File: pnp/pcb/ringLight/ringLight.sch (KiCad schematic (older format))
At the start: 13 parts, among them J1 Conn_01x03_Male, J2 Conn_01x03_Male

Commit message: Add LCSC PNs to Ringlight
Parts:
- J1: LCSC (none) -> C146126
- J2: LCSC (none) -> C141812
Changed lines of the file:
@@
 F 2 "Connector_JST:JST_PH_B3B-PH-SM4-TB_1x03-1MP_P2.00mm_Vertical" H 1050 1150 50  0001 C CNN
 F 3 "~" H 1050 1150 50  0001 C CNN
+F 4 "C141812" H 1050 1150 50  0001 C CNN "LCSC"
 	1    1050 1150
 	1    0    0    -1
@@
 F 2 "Connector_JST:JST_PH_B3B-PH-SM4-TB_1x03-1MP_P2.00mm_Vertical" H 725 1150 50  0001 C CNN
 F 3 "~" H 725 1150 50  0001 C CNN
+F 4 "C146126" H 725 1150 50  0001 C CNN "LCSC"
 	1    725  1150
 	1    0    0    -1

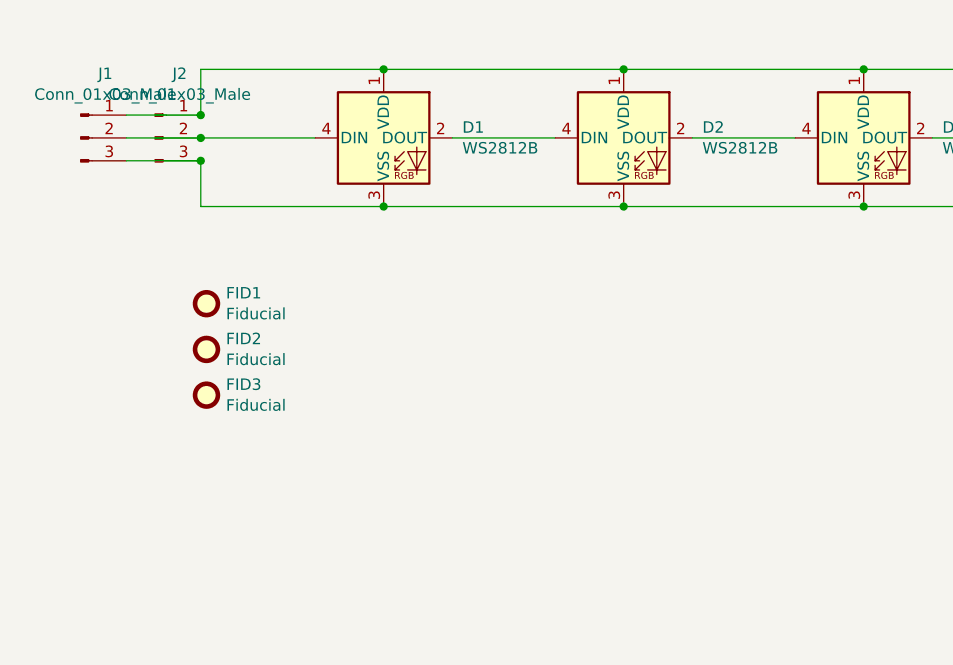
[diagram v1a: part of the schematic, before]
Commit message: updated ring light to rev03. changed connector pinout to match motherboard. switched to THT for connector that works with both right angle and straight up to be compatible with both board orientations. increased fiducial size. added decoupling capacitor.
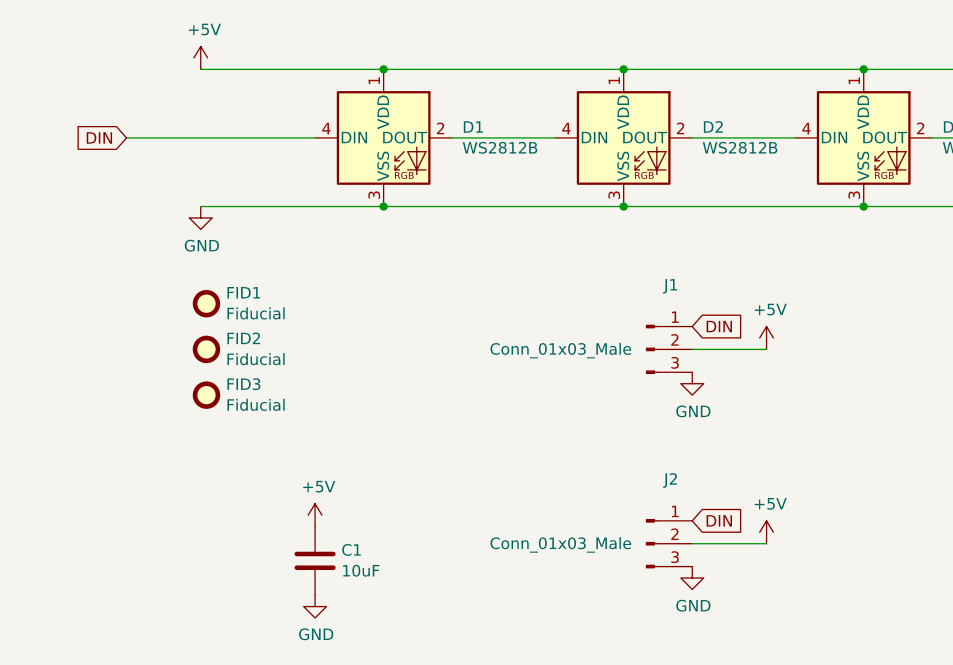
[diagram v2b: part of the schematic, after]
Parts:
- added C1: 10uF, Capacitor_SMD:C_0805_2012Metric, symbol Device:C
- FID1, FID2, FID3: footprint Fiducial:Fiducial_0.5mm_Mask1mm -> Fiducial:Fiducial_1mm_Mask2mm
- J1: footprint Connector_JST:JST_PH_B3B-PH-SM4-TB_1x03-1MP_P2.00mm_Vertical -> Connector_JST:JST_XH_B3B-XH-A_1x03_P2.50mm_Vertical
- J2: footprint Connector_JST:JST_PH_B3B-PH-SM4-TB_1x03-1MP_P2.00mm_Vertical -> index:S3B-XH-SM4-TB
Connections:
- net +5V: now reaches D1.1 (VDD), D2.1 (VDD), D3.1 (VDD), D4.1 (VDD), D5.1 (VDD), D6.1 (VDD), D7.1 (VDD), D8.1 (VDD)
- net +5V: now also J1.2 (Pin_2), J2.2 (Pin_2), C1.1; no longer J1.1 (Pin_1), J2.1 (Pin_1)
- net GND: now reaches D1.3 (VSS), D2.3 (VSS), D3.3 (VSS), D4.3 (VSS), D5.3 (VSS), D6.3 (VSS), D7.3 (VSS), D8.3 (VSS), J1.3 (Pin_3), J2.3 (Pin_3)
- net GND: now also C1.2
- new net DIN: D1.4 (DIN), J1.1 (Pin_1), J2.1 (Pin_1)
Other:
- moved on the sheet: J1, J2
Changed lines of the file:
@@
 L Connector:Conn_01x03_Male J2
 U 1 1 5EDD8ED7
-P 1050 1150
-F 0 "J2" H 1158 1431 50  0000 C CNN
-F 1 "Conn_01x03_Male" H 1158 1340 50  0000 C CNN
-F 2 "Connector_JST:JST_PH_B3B-PH-SM4-TB_1x03-1MP_P2.00mm_Vertical" H 1050 1150 50  0001 C CNN
-F 3 "~" H 1050 1150 50  0001 C CNN
-F 4 "C141812" H 1050 1150 50  0001 C CNN "LCSC"
-	1    1050 1150
+P 3200 2925
+F 0 "J2" H 3308 3206 50  0000 C CNN
+F 1 "Conn_01x03_Male" H 2825 2925 50  0000 C CNN
+F 2 "index:S3B-XH-SM4-TB" H 3200 2925 50  0001 C CNN
+F 3 "~" H 3200 2925 50  0001 C CNN
+F 4 "C141812" H 3200 2925 50  0001 C CNN "LCSC"
+	1    3200 2925
 	1    0    0    -1
 $EndComp
@@
 $EndComp
 Wire Wire Line
-	1250 1150 1750 1150
-Wire Wire Line
-	1250 1250 1250 1450
-Wire Wire Line
 	1250 1450 2050 1450
 Wire Wire Line
@@
 Wire Wire Line
 	8650 1150 9100 1150
-Wire Wire Line
-	1250 850  1250 1050
 $Comp
 L Mechanical:Fiducial FID1
@@
 F 0 "FID1" H 1360 1921 50  0000 L CNN
 F 1 "Fiducial" H 1360 1830 50  0000 L CNN
-F 2 "Fiducial:Fiducial_0.5mm_Mask1mm" H 1275 1875 50  0001 C CNN
+F 2 "Fiducial:Fiducial_1mm_Mask2mm" H 1275 1875 50  0001 C CNN
 F 3 "~" H 1275 1875 50  0001 C CNN
 	1    1275 1875
@@
 F 0 "FID2" H 1360 2121 50  0000 L CNN
 F 1 "Fiducial" H 1360 2030 50  0000 L CNN
-F 2 "Fiducial:Fiducial_0.5mm_Mask1mm" H 1275 2075 50  0001 C CNN
+F 2 "Fiducial:Fiducial_1mm_Mask2mm" H 1275 2075 50  0001 C CNN
 F 3 "~" H 1275 2075 50  0001 C CNN
 	1    1275 2075
@@
 F 0 "FID3" H 1360 2321 50  0000 L CNN
 F 1 "Fiducial" H 1360 2230 50  0000 L CNN
-F 2 "Fiducial:Fiducial_0.5mm_Mask1mm" H 1275 2275 50  0001 C CNN
+F 2 "Fiducial:Fiducial_1mm_Mask2mm" H 1275 2275 50  0001 C CNN
 F 3 "~" H 1275 2275 50  0001 C CNN
 	1    1275 2275
@@
 L Connector:Conn_01x03_Male J1
 U 1 1 607E080D
-P 725 1150
-F 0 "J1" H 833 1431 50  0000 C CNN
-F 1 "Conn_01x03_Male" H 833 1340 50  0000 C CNN
-F 2 "Connector_JST:JST_PH_B3B-PH-SM4-TB_1x03-1MP_P2.00mm_Vertical" H 725 1150 50  0001 C CNN
-F 3 "~" H 725 1150 50  0001 C CNN
-F 4 "C146126" H 725 1150 50  0001 C CNN "LCSC"
-	1    725  1150
-	1    0    0    -1
-$EndComp
-Wire Wire Line
-	925  1050 1250 1050
-Connection ~ 1250 1050
-Wire Wire Line
-	925  1150 1250 1150
-Connection ~ 1250 1150
-Wire Wire Line
-	925  1250 1250 1250
-Connection ~ 1250 1250
+P 3200 2075
+F 0 "J1" H 3308 2356 50  0000 C CNN
+F 1 "Conn_01x03_Male" H 2825 2075 50  0000 C CNN
+F 2 "Connector_JST:JST_XH_B3B-XH-A_1x03_P2.50mm_Vertical" H 3200 2075 50  0001 C CNN
+F 3 "~" H 3200 2075 50  0001 C CNN
+F 4 "C146126" H 3200 2075 50  0001 C CNN "LCSC"
+	1    3200 2075
+	1    0    0    -1
+$EndComp
+$Comp
+L power:GND #PWR0101
+U 1 1 6138B926
+P 1250 1450
+F 0 "#PWR0101" H 1250 1200 50  0001 C CNN
+F 1 "GND" H 1255 1277 50  0000 C CNN
+F 2 "" H 1250 1450 50  0001 C CNN
+F 3 "" H 1250 1450 50  0001 C CNN
+	1    1250 1450
+	1    0    0    -1
+$EndComp
+Wire Wire Line
+	925  1150 1750 1150
+$Comp
+L power:+5V #PWR0102
+U 1 1 6138DF18
+P 1250 850
+F 0 "#PWR0102" H 1250 700 50  0001 C CNN
+F 1 "+5V" H 1265 1023 50  0000 C CNN
+F 2 "" H 1250 850 50  0001 C CNN
+F 3 "" H 1250 850 50  0001 C CNN
+	1    1250 850
+	1    0    0    -1
+$EndComp
+Text GLabel 925  1150 0    50   Input ~ 0
+DIN
+$Comp
+L power:GND #PWR0103
+U 1 1 613949B9
+P 3400 3025
+F 0 "#PWR0103" H 3400 2775 50  0001 C CNN
+F 1 "GND" H 3405 2852 50  0000 C CNN
+F 2 "" H 3400 3025 50  0001 C CNN
+F 3 "" H 3400 3025 50  0001 C CNN
+	1    3400 3025
+	1    0    0    -1
+$EndComp
+$Comp
+L power:GND #PWR0104
+U 1 1 61394DE1
+P 3400 2175
+F 0 "#PWR0104" H 3400 1925 50  0001 C CNN
+F 1 "GND" H 3405 2002 50  0000 C CNN
+F 2 "" H 3400 2175 50  0001 C CNN
+F 3 "" H 3400 2175 50  0001 C CNN
+	1    3400 2175
+	1    0    0    -1
+$EndComp
+$Comp
+L power:+5V #PWR0105
+U 1 1 6139851D
+P 3725 2075
+F 0 "#PWR0105" H 3725 1925 50  0001 C CNN
+F 1 "+5V" H 3740 2248 50  0000 C CNN
+F 2 "" H 3725 2075 50  0001 C CNN
+F 3 "" H 3725 2075 50  0001 C CNN
+	1    3725 2075
+	1    0    0    -1
+$EndComp
+$Comp
+L power:+5V #PWR0106
+U 1 1 61398B51
+P 3725 2925
+F 0 "#PWR0106" H 3725 2775 50  0001 C CNN
+F 1 "+5V" H 3740 3098 50  0000 C CNN
+F 2 "" H 3725 2925 50  0001 C CNN
+F 3 "" H 3725 2925 50  0001 C CNN
+	1    3725 2925
+	1    0    0    -1
+$EndComp
+Wire Wire Line
+	3400 2925 3725 2925
+Wire Wire Line
+	3400 2075 3725 2075
+Text GLabel 3400 1975 2    50   Input ~ 0
+DIN
+Text GLabel 3400 2825 2    50   Input ~ 0
+DIN
+$Comp
+L Device:C C1
+U 1 1 613B8E1E
+P 1750 3000
+F 0 "C1" H 1865 3046 50  0000 L CNN
+F 1 "10uF" H 1865 2955 50  0000 L CNN
+F 2 "Capacitor_SMD:C_0805_2012Metric" H 1788 2850 50  0001 C CNN
+F 3 "~" H 1750 3000 50  0001 C CNN
+	1    1750 3000
+	1    0    0    -1
+$EndComp
+$Comp
+L power:+5V #PWR0107
+U 1 1 613B9153
+P 1750 2850
+F 0 "#PWR0107" H 1750 2700 50  0001 C CNN
+F 1 "+5V" H 1765 3023 50  0000 C CNN
+F 2 "" H 1750 2850 50  0001 C CNN
+F 3 "" H 1750 2850 50  0001 C CNN
+	1    1750 2850
+	1    0    0    -1
+$EndComp
+$Comp
+L power:GND #PWR0108
+U 1 1 613B975A
+P 1750 3150
+F 0 "#PWR0108" H 1750 2900 50  0001 C CNN
+F 1 "GND" H 1755 2977 50  0000 C CNN
+F 2 "" H 1750 3150 50  0001 C CNN
+F 3 "" H 1750 3150 50  0001 C CNN
+	1    1750 3150
+	1    0    0    -1
+$EndComp
 $EndSCHEMATC

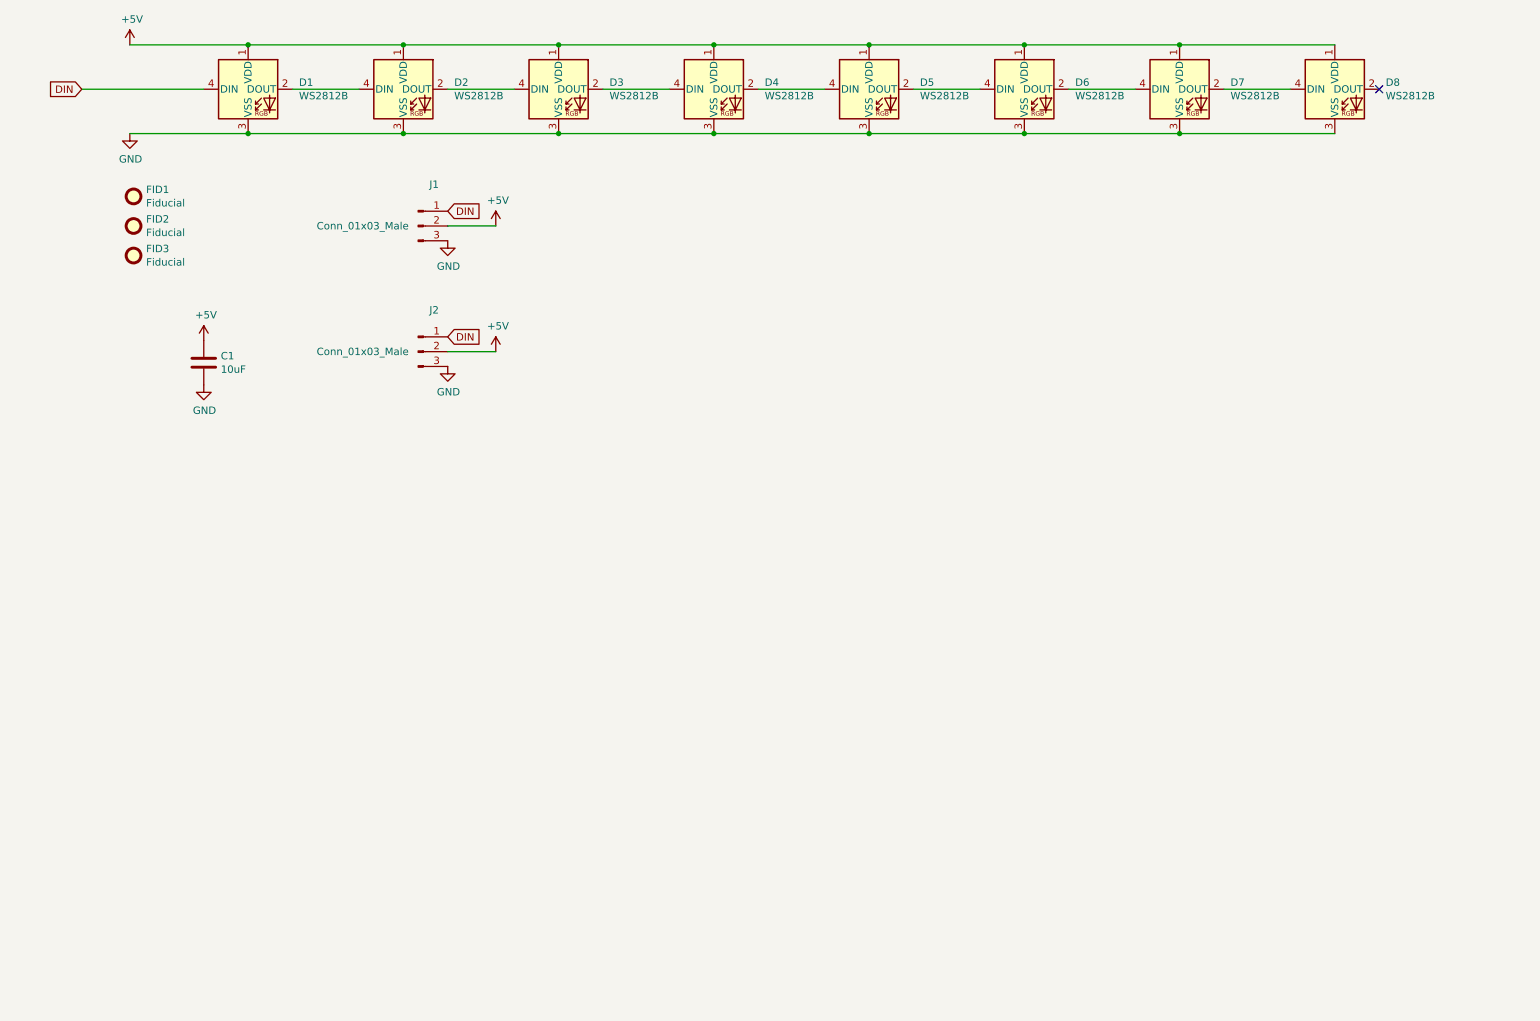
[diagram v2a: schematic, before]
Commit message: Ring Light Rev 04 - new schematic and pcb
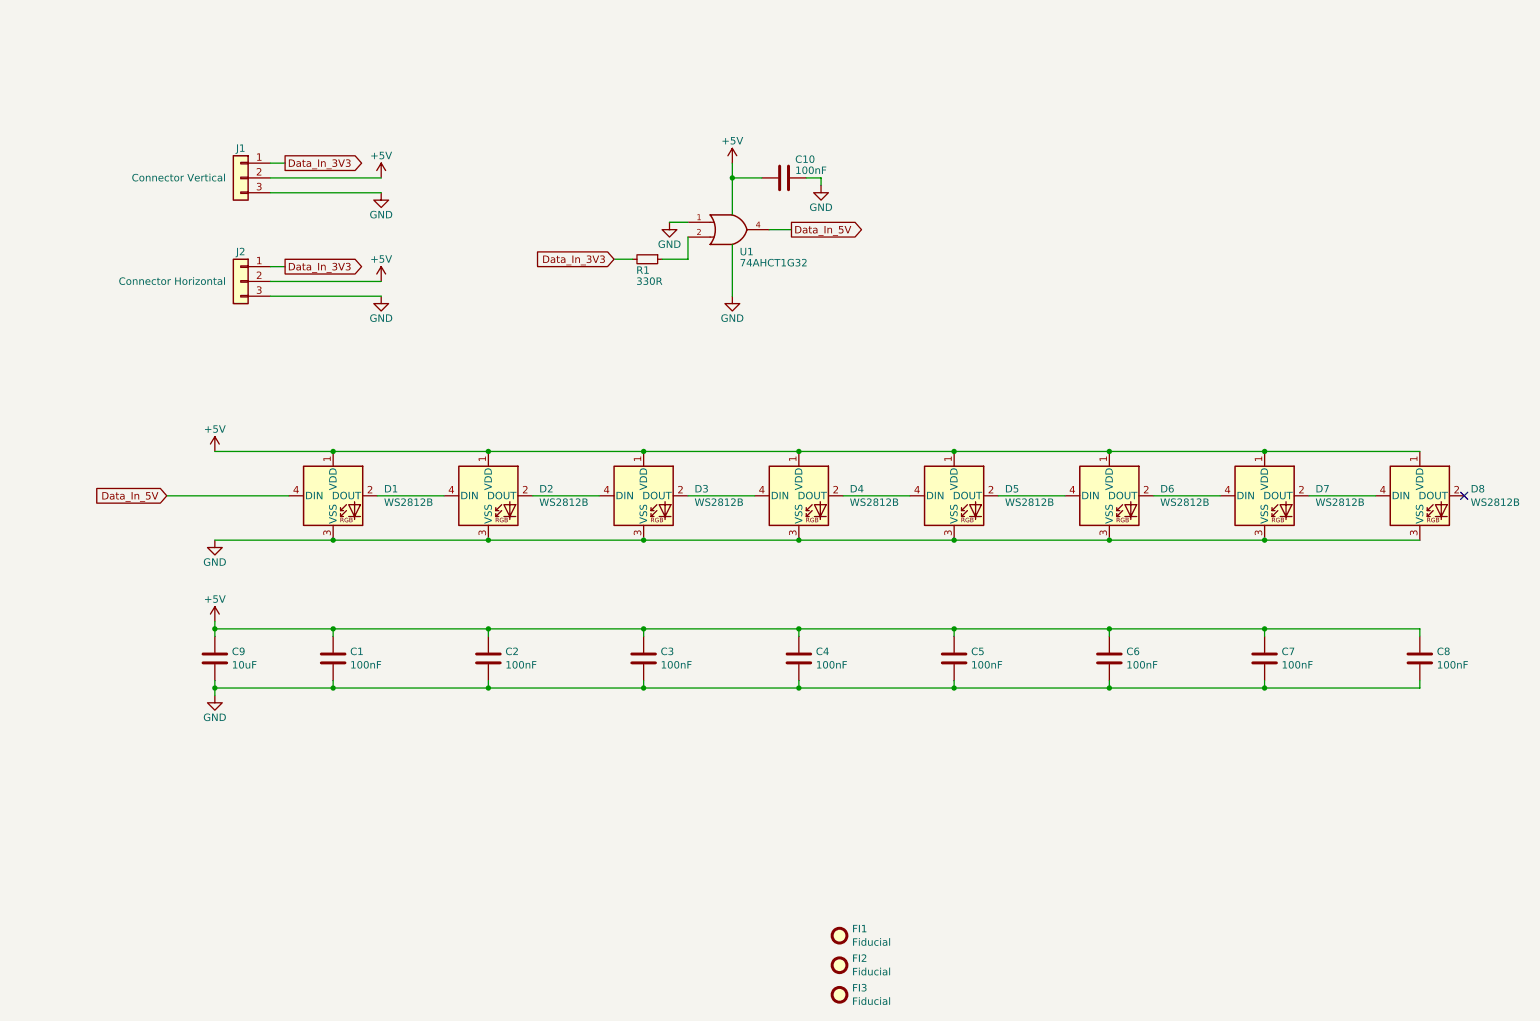
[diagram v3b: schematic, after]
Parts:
- removed J1: Conn_01x03_Male, Connector_JST:JST_XH_B3B-XH-A_1x03_P2.50mm_Vertical, symbol Connector:Conn_01x03_Male
- removed J2: Conn_01x03_Male, index:S3B-XH-SM4-TB, symbol Connector:Conn_01x03_Male
- added C1, C10, C2, C3, C4, C5, C6, C7, C8: 100nF, Capacitor_SMD:C_0805_2012Metric, symbol Device:C
- added J1: Connector Vertical, Connector_JST:JST_XH_B3B-XH-A_1x03_P2.50mm_Vertical, symbol Connector_Generic:Conn_01x03
- added J2: Connector Horizontal, Connector_JST:JST_XH_S3B-XH-A-1_1x03_P2.50mm_Horizontal, symbol Connector_Generic:Conn_01x03
- added R1: 330R, Resistor_SMD:R_0805_2012Metric, symbol Device:R_Small
- added U1: 74AHCT1G32, Package_TO_SOT_SMD:SOT-23-5, symbol 74xGxx:74AHCT1G32
- C9: renamed from C1; footprint Capacitor_SMD:C_0805_2012Metric -> Capacitor_SMD:C_1206_3216Metric; JLCPCB (none) -> C13585; LCSC (none) -> C13585; Part # (none) -> CL31A106KBHNNNE
- D1, D2, D3, D4, D5, D6, D7, D8: Part # (none) -> WS2812B
- renumbered FID1 to FI1, FID2 to FI2, FID3 to FI3
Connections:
- net +5V: now also C1.1, C10.1, C2.1, C3.1, C4.1, C5.1, C6.1, C7.1, C8.1, J1.2 (Pin_2), J2.2 (Pin_2), U1.5 (VCC)
- net GND: now also C1.2, C10.2, C2.2, C3.2, C4.2, C5.2, C6.2, C7.2, C8.2, J1.3 (Pin_3), J2.3 (Pin_3), U1.1, U1.3 (GND)
- net DIN renamed Data_In_5V
- net Data_In_5V: now also U1.4
- new net: R1.1, U1.2
- new net Data_In_3V3: J1.1 (Pin_1), J2.1 (Pin_1), R1.2
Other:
- moved on the sheet: C9, D1, D2, D3, D4, D5, D6, D7, D8, FI1, FI2, FI3
